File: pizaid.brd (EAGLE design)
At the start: 55.2 x 49.5 mm, 37 parts, among them X1 S4B-ZR

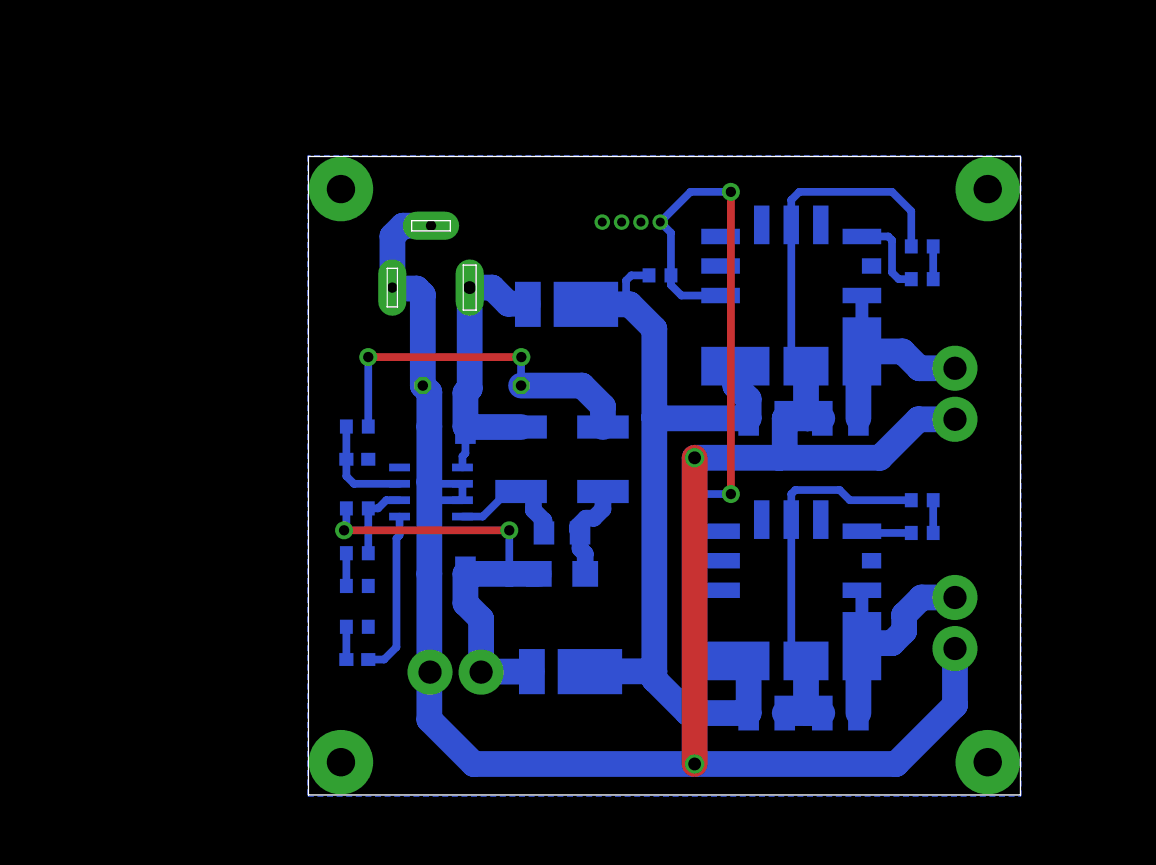
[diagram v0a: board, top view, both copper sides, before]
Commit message: supported Raspberry Pi model B+
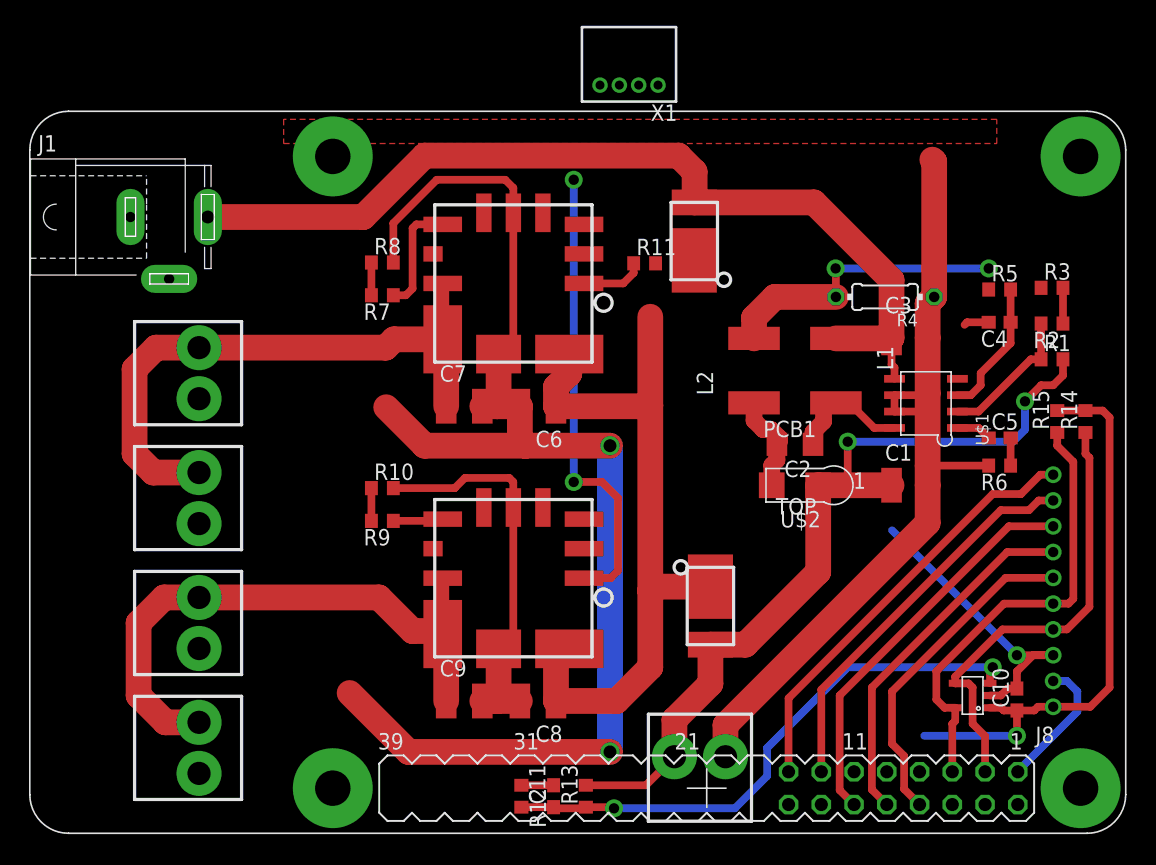
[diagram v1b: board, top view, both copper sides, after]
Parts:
- removed U$11, U$12, U$13, U$3: M2, pizaid:M2
- added C10, C11: (no value), rcl:C0603
- added PCB1: RASPBERRY_PI_B+, pizaid:RASPBERRY_PI_B+
- added R12, R13, R14, R15: (no value), rcl:R0603
- added S1: 10B-PH, con-jst:S10B-PH
- added U$14, U$15: B2P-VH, pizaid:B2P-VH
- added U$16: MCP3021, pizaid:SOT-23
- moved U$9 59.4 mm to (16.6, 10.0), flipped to the top
- moved U$8 59.2 mm to (16.6, 29.4), flipped to the top
- moved R3 58.6 mm to (82.7, 45.7), flipped to the top
- moved R2 56.8 mm to (82.7, 42.9), flipped to the top
- moved R1 55.1 mm to (82.7, 40.1), flipped to the top
- moved C5 52.7 mm to (78.7, 34.0), flipped to the top
- moved R6 51.4 mm to (78.7, 31.9), flipped to the top
- moved C4 50.9 mm to (78.7, 43.0), flipped to the top
- moved R5 50.9 mm to (78.7, 45.5), flipped to the top
- moved R7 41.9 mm to (30.8, 45.1), flipped to the top
- moved R8 41.9 mm to (30.8, 47.6), flipped to the top
- moved R10 41.9 mm to (30.8, 30.1), flipped to the top
- moved R9 41.9 mm to (30.8, 27.6), flipped to the top
- moved U$1 39.0 mm to (72.9, 36.7), flipped to the top
- moved C1 36.5 mm to (71.7, 30.4), flipped to the top
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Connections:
- new net 3V3@1: PCB1.1, S1.P$2
- new net 5V0@2: C10.1, C9.1, PCB1.2, PCB1.4, R14.2, R15.2, S1.P$1, U$14.P$1, U$16.P$1, U$7.P$4, U$7.P$5, U$9.P$1
- new net GND@1: PCB1.9
- new net GND@4: PCB1.14, PCB1.6
- new net JNET: C7.1, U$15.P$1, U$6.P$4, U$6.P$5, U$8.P$1
- new net N$13: PCB1.8, S1.P$6
- new net N$16: PCB1.5, R15.1, S1.P$5, U$16.P$5
- new net N$20: PCB1.3, R14.1, S1.P$4, U$16.P$4
- new net N$21: PCB1.10, S1.P$7
- new net N$22: PCB1.12, S1.P$8
- new net N$23: PCB1.13, S1.P$9
- net GND: now also C10.2, C11.2, PCB1.PE_BL, PCB1.PE_BR, PCB1.PE_TL, PCB1.PE_TR, R12.1, S1.P$3, U$14.P$2, U$15.P$2, U$16.P$2; no longer U$11.P$1, U$12.P$1, U$13.P$1, U$3.P$1
- net N$19: now also C11.1, R12.2, R13.1, U$16.P$3; no longer C7.1, U$6.P$4, U$6.P$5, U$8.P$1
- net N$3: now also R13.2
- net N$9: now also PCB1.15, S1.P$10; no longer C9.1, U$7.P$4, U$7.P$5, U$9.P$1
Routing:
- net 5V0@2: track 0.00 -> 90.9 mm, vias 0 -> 1
- net VCC: track 23.6 -> 72.5 mm
- net JNET: track 0.00 -> 46.7 mm
- net N$16: track 0.00 -> 35.3 mm
- net N$20: track 0.00 -> 35.2 mm
- net N$22: track 0.00 -> 30.9 mm
- net N$23: track 0.00 -> 30.4 mm
- net N$3: track 35.7 -> 65.5 mm
- net N$21: track 0.00 -> 28.0 mm
- net N$19: track 17.4 -> 44.1 mm, vias 0 -> 2
- net N$13: track 0.00 -> 25.8 mm
- net GND: track 207.2 -> 221.7 mm, vias 2 -> 3
- net N$9: track 19.2 -> 33.4 mm
- net N$12: track 51.8 -> 40.8 mm
- net 3V3@1: track 0.00 -> 10.4 mm
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- added copper zone on layer 1, net GND
- removed copper zone on layer 16, net GND
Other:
- board size 55.2 x 49.5 mm -> 6.9 x 6.9 mm

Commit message: added gerber and con-jst.lbr
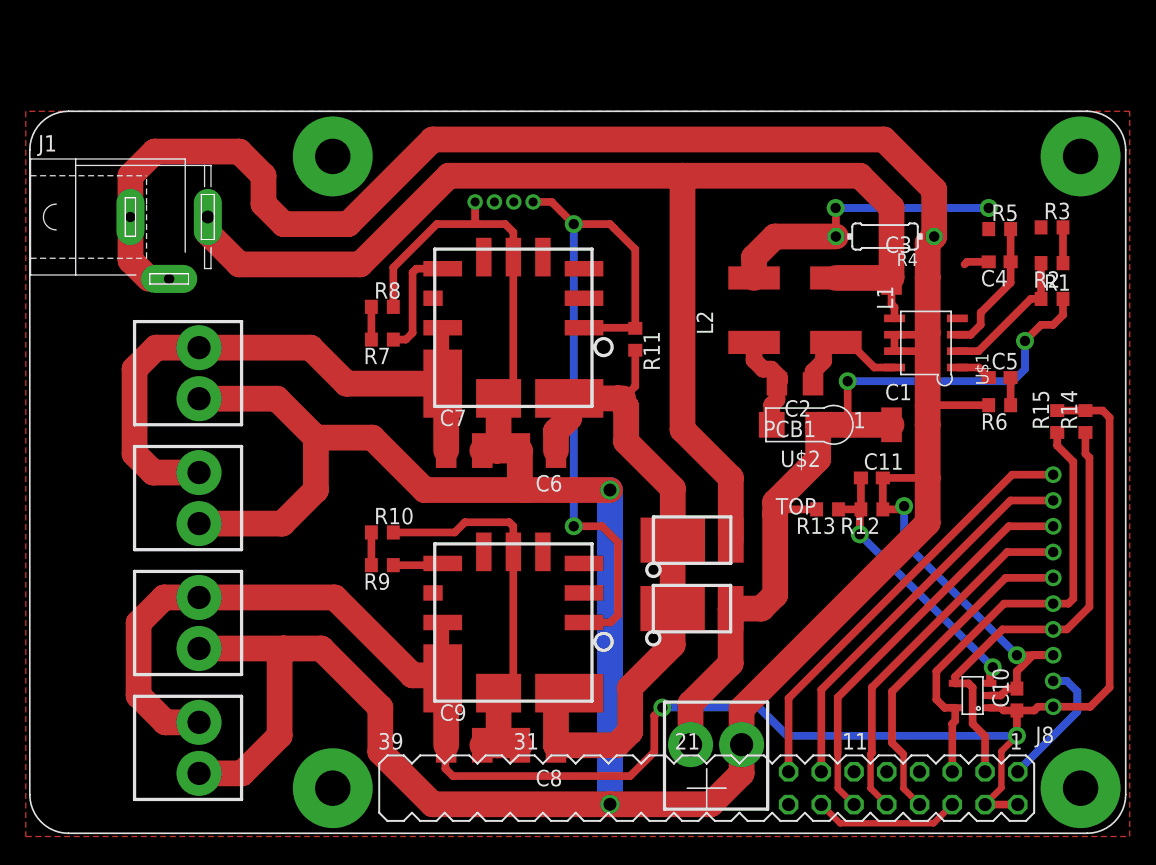
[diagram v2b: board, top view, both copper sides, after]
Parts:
- moved R12 35.1 mm to (68.8, 28.5), turned to 180 degrees
- moved C11 34.9 mm to (68.8, 30.9), turned to 0 degrees
- moved R13 29.1 mm to (65.3, 28.5), turned to 180 degrees
- moved U$5 23.2 mm to (54.8, 26.1), turned to 180 degrees
- moved X1 13.3 mm to (40.2, 52.3), flipped to the bottom
- moved R11 5.94 mm to (50.4, 41.7), turned to 270 degrees
- moved C2 4.69 mm to (62.8, 38.2)
- moved C3 4.69 mm to (71.7, 46.5)
- moved C4 4.69 mm to (78.7, 47.7)
- moved C5 4.69 mm to (78.7, 38.7)
- moved L1 4.69 mm to (66.0, 43.9)
- moved L2 4.69 mm to (59.6, 43.9)
- moved R1 4.69 mm to (82.7, 44.8)
- moved R2 4.69 mm to (82.7, 47.6)
- moved R3 4.69 mm to (82.7, 50.4)
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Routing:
- net GND: track 221.7 -> 385.4 mm, vias 3 -> 4
- net 5V0@2: track 90.9 -> 145.3 mm, vias 1 -> 2
- net VCC: track 72.5 -> 102.0 mm
- net N$19: track 44.1 -> 22.1 mm
- net N$12: track 40.8 -> 55.5 mm
- net GND@4: track 0.00 -> 11.4 mm
- net N$8: track 56.7 -> 52.4 mm
- net N$3: track 65.5 -> 64.1 mm
- net JNET: track 46.7 -> 47.6 mm

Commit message: added part info
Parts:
- C1: value (none) -> 22u
- C10, C11, C5: value (none) -> 0.1u
- C2: value (none) -> 2.2u
- C4: value (none) -> 0.22u
- C6, C8: value (none) -> 22u25V
- C7, C9: value (none) -> 22u16V
- L1, L2: value (none) -> 33u
- R1: value (none) -> 100k
- R10, R8: value (none) -> 330
- R12, R13, R2: value (none) -> 10k
- R14, R15, R3: value (none) -> 2.2k
- R4: value (none) -> 0.2
- R5: value (none) -> 24
- R6, R7, R9: value (none) -> 1k
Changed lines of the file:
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@@
 <elements>
 <element name="U$1" library="pizaid" package="SOP8" value="LT1512CS8" x="72.945" y="41.4075" rot="R90"/>
-<element name="R1" library="rcl" package="R0603" value="" x="82.7225" y="44.825"/>
-<element name="R2" library="rcl" package="R0603" value="" x="82.7225" y="47.5975" rot="R180"/>
-<element name="R3" library="rcl" package="R0603" value="" x="82.7225" y="50.37"/>
-<element name="R4" library="rcl" package="0204/7" value="" x="69.77" y="49.6625" rot="R180"/>
-<element name="R5" library="rcl" package="R0603" value="" x="78.66" y="50.2375"/>
-<element name="R6" library="rcl" package="R0603" value="" x="78.66" y="36.58" rot="R180"/>
-<element name="C1" library="rcl" package="C3225" value="" x="71.675" y="35.0575"/>
-<element name="C2" library="rcl" package="C3216" value="" x="62.785" y="38.2325" rot="R180"/>
+<element name="R1" library="rcl" package="R0603" value="100k" x="82.7225" y="44.825"/>
+<element name="R2" library="rcl" package="R0603" value="10k" x="82.7225" y="47.5975" rot="R180"/>
+<element name="R3" library="rcl" package="R0603" value="2.2k" x="82.7225" y="50.37"/>
+<element name="R4" library="rcl" package="0204/7" value="0.2" x="69.77" y="49.6625" rot="R180"/>
+<element name="R5" library="rcl" package="R0603" value="24" x="78.66" y="50.2375"/>
+<element name="R6" library="rcl" package="R0603" value="1k" x="78.66" y="36.58" rot="R180"/>
+<element name="C1" library="rcl" package="C3225" value="22u" x="71.675" y="35.0575"/>
+<element name="C2" library="rcl" package="C3216" value="2.2u" x="62.785" y="38.2325" rot="R180"/>
 <element name="C3" library="rcl" package="C3225" value="22u" x="71.675" y="46.4875"/>
-<element name="C4" library="rcl" package="C0603" value="" x="78.66" y="47.6975" rot="R180"/>
-<element name="C5" library="rcl" package="C0603" value="" x="78.66" y="38.7275"/>
-<element name="L1" library="rcl" package="L5650M" value="" x="65.96" y="43.9475" rot="R270"/>
-<element name="L2" library="rcl" package="L5650M" value="" x="59.61" y="43.9475" rot="R90"/>
+<element name="C4" library="rcl" package="C0603" value="0.22u" x="78.66" y="47.6975" rot="R180"/>
+<element name="C5" library="rcl" package="C0603" value="0.1u" x="78.66" y="38.7275"/>
+<element name="L1" library="rcl" package="L5650M" value="33u" x="65.96" y="43.9475" rot="R270"/>
+<element name="L2" library="rcl" package="L5650M" value="33u" x="59.61" y="43.9475" rot="R90"/>
 <element name="U$2" library="pizaid" package="SOD-123FL" value="SS2040FL" x="62.785" y="35.0575" rot="R180"/>
 <element name="J1" library="pizaid" package="SPC4077" value="" x="14.2425" y="51.175">
@@
 <element name="U$6" library="pizaid" package="OKL-T/6" value="OKL-T/6" x="40.9425" y="42.585" rot="R180"/>
 <element name="U$7" library="pizaid" package="OKL-T/6" value="OKL-T/6" x="40.9425" y="19.725" rot="R180"/>
-<element name="C6" library="rcl" package="C3225" value="" x="42.8475" y="33.06" rot="R180"/>
-<element name="C7" library="rcl" package="C3225" value="" x="37.1325" y="33.06"/>
-<element name="C8" library="rcl" package="C3225" value="" x="42.8475" y="10.2" rot="R180"/>
-<element name="C9" library="rcl" package="C3225" value="" x="37.1325" y="10.2"/>
-<element name="R7" library="rcl" package="R0603" value="" x="30.7825" y="41.6675" rot="R180"/>
-<element name="R8" library="rcl" package="R0603" value="" x="30.7825" y="44.2075"/>
-<element name="R9" library="rcl" package="R0603" value="" x="30.7825" y="24.17" rot="R180"/>
-<element name="R10" library="rcl" package="R0603" value="" x="30.7825" y="26.71"/>
+<element name="C6" library="rcl" package="C3225" value="22u25V" x="42.8475" y="33.06" rot="R180"/>
+<element name="C7" library="rcl" package="C3225" value="22u16V" x="37.1325" y="33.06"/>
+<element name="C8" library="rcl" package="C3225" value="22u25V" x="42.8475" y="10.2" rot="R180"/>
+<element name="C9" library="rcl" package="C3225" value="22u16V" x="37.1325" y="10.2"/>
+<element name="R7" library="rcl" package="R0603" value="1k" x="30.7825" y="41.6675" rot="R180"/>
+<element name="R8" library="rcl" package="R0603" value="330" x="30.7825" y="44.2075"/>
+<element name="R9" library="rcl" package="R0603" value="1k" x="30.7825" y="24.17" rot="R180"/>
+<element name="R10" library="rcl" package="R0603" value="330" x="30.7825" y="26.71"/>
 <element name="X1" library="con-jst" package="S4B-ZR" value="S4B-ZR" x="40.225" y="52.3425" rot="MR180">
 <attribute name="OC_NEWARK" value="38K8076" x="40.225" y="52.3425" size="1.778" layer="28" rot="MR180" display="off"/>
@@
 <element name="U$15" library="pizaid" package="B2P-VH" value="B2P-VH" x="16.5625" y="39.0625" rot="R270"/>
 <element name="U$16" library="pizaid" package="SOT-23" value="MCP3021" x="76.5625" y="14.0625" rot="R90"/>
-<element name="C10" library="rcl" package="C0603" value="" x="80" y="13.75" rot="R90"/>
-<element name="C11" library="rcl" package="C0603" value="" x="68.75" y="30.9375"/>
-<element name="R12" library="rcl" package="R0603" value="" x="68.75" y="28.5" rot="R180"/>
-<element name="R13" library="rcl" package="R0603" value="" x="65.3125" y="28.5" rot="R180"/>
-<element name="R14" library="rcl" package="R0603" value="" x="85.3125" y="35.3125" rot="R90"/>
-<element name="R15" library="rcl" package="R0603" value="" x="83.125" y="35.3125" rot="R90"/>
+<element name="C10" library="rcl" package="C0603" value="0.1u" x="80" y="13.75" rot="R90"/>
+<element name="C11" library="rcl" package="C0603" value="0.1u" x="68.75" y="30.9375"/>
+<element name="R12" library="rcl" package="R0603" value="10k" x="68.75" y="28.5" rot="R180"/>
+<element name="R13" library="rcl" package="R0603" value="10k" x="65.3125" y="28.5" rot="R180"/>
+<element name="R14" library="rcl" package="R0603" value="2.2k" x="85.3125" y="35.3125" rot="R90"/>
+<element name="R15" library="rcl" package="R0603" value="2.2k" x="83.125" y="35.3125" rot="R90"/>
 <element name="PCB1" library="pizaid" package="RASPBERRY_PI_B+" value="RASPBERRY_PI_B+" x="88.4375" y="59.375" rot="R180"/>
 </elements>

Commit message: changed dcjack
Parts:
- removed J1: (no value), pizaid:SPC4077
- added X2: DCJACK-R, kamiki-dcjack:2DC-0005D100-R
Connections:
- net GND: now also X2.2, X2.3; no longer J1.1, J1.2
- net VCC: now also X2.1; no longer J1.3
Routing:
- net VCC: track 102.0 -> 101.5 mm
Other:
- board outline removed
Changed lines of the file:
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@@
 <element name="L2" library="rcl" package="L5650M" value="33u" x="59.61" y="43.9475" rot="R90"/>
 <element name="U$2" library="pizaid" package="SOD-123FL" value="SS2040FL" x="62.785" y="35.0575" rot="R180"/>
-<element name="J1" library="pizaid" package="SPC4077" value="" x="14.2425" y="51.175">
-<attribute name="OC_NEWARK" value="unknown" x="14.2425" y="51.175" size="1.778" layer="27" display="off"/>
-<attribute name="MPN" value="" x="14.2425" y="51.175" size="1.778" layer="27" display="off"/>
-<attribute name="MF" value="" x="14.2425" y="51.175" size="1.778" layer="27" display="off"/>
-<attribute name="OC_FARNELL" value="unknown" x="14.2425" y="51.175" size="1.778" layer="27" display="off"/>
-</element>
 <element name="U$4" library="pizaid" package="POWERDI5" value="SBR15U50" x="54.795" y="20.8025" rot="R180"/>
 <element name="U$5" library="pizaid" package="POWERDI5" value="SBR15U50" x="54.8075" y="26.1125" rot="R180"/>
@@
 <element name="R15" library="rcl" package="R0603" value="2.2k" x="83.125" y="35.3125" rot="R90"/>
 <element name="PCB1" library="pizaid" package="RASPBERRY_PI_B+" value="RASPBERRY_PI_B+" x="88.4375" y="59.375" rot="R180"/>
+<element name="X2" library="kamiki-dcjack" package="2DC-0005D100-R" value="DCJACK-R" x="13.4375" y="51.5625"/>
 </elements>
 <signals>
@@
 <contactref element="C1" pad="2"/>
 <contactref element="R3" pad="1"/>
-<contactref element="J1" pad="2"/>
-<contactref element="J1" pad="1"/>
 <contactref element="U$6" pad="P$3"/>
 <contactref element="U$7" pad="P$3"/>
@@
 <wire x1="25.625" y1="34.0625" x2="22.605" y2="37.0825" width="2" layer="1"/>
 <wire x1="16.5625" y1="37.0825" x2="22.605" y2="37.0825" width="2" layer="1"/>
-<wire x1="11.2425" y1="51.175" x2="11.2425" y2="54.3675" width="2" layer="1"/>
 <wire x1="11.2425" y1="54.3675" x2="13.125" y2="56.25" width="2" layer="1"/>
 <wire x1="13.125" y1="56.25" x2="19.6875" y2="56.25" width="2" layer="1"/>
@@
 <wire x1="69.6875" y1="57.1875" x2="73.58" y2="53.295" width="2" layer="1"/>
 <wire x1="73.58" y1="49.6625" x2="73.58" y2="53.295" width="2" layer="1"/>
-<wire x1="12.6875" y1="46.375" x2="11.25" y2="47.8125" width="2" layer="1"/>
-<wire x1="11.25" y1="47.8125" x2="11.25" y2="51.1825" width="2" layer="1"/>
-<wire x1="11.25" y1="51.5625" x2="11.25" y2="51.1825" width="2" layer="1"/>
-<wire x1="11.25" y1="51.1825" x2="11.2425" y2="51.175" width="2" layer="1"/>
 <wire x1="25.625" y1="34.0625" x2="30" y2="34.0625" width="2" layer="1"/>
 <wire x1="48.4375" y1="5.625" x2="56.25" y2="5.625" width="2" layer="1"/>
@@
 <wire x1="37.975" y1="52.3425" x2="37.975" y2="50.775" width="0.6" layer="1"/>
 <wire x1="37.975" y1="50.775" x2="38.125" y2="50.625" width="0.6" layer="1"/>
+<contactref element="X2" pad="2"/>
+<contactref element="X2" pad="3"/>
+<wire x1="11.1875" y1="51.5625" x2="11.2425" y2="51.6175" width="2" layer="1"/>
+<wire x1="11.2425" y1="51.6175" x2="11.2425" y2="54.3675" width="2" layer="1"/>
+<wire x1="11.1875" y1="51.5625" x2="11.1875" y2="49.7625" width="2" layer="1"/>
+<wire x1="11.1875" y1="49.7625" x2="14.1875" y2="46.7625" width="2" layer="1"/>
 <wire x1="41.875" y1="30" x2="40.625" y2="27.5" width="0" layer="19" extent="1-1"/>
 </signal>
@@
 <contactref element="L1" pad="1"/>
 <contactref element="U$1" pad="5"/>
-<contactref element="J1" pad="3"/>
 <contactref element="U$5" pad="P$2"/>
 <wire x1="65.96" y1="46.4475" x2="70.235" y2="46.4475" width="2" layer="1"/>
@@
 <wire x1="54.0625" y1="54.375" x2="35.9375" y2="54.375" width="2" layer="1"/>
 <wire x1="35.9375" y1="54.375" x2="29.0625" y2="47.5" width="2" layer="1"/>
-<wire x1="29.0625" y1="47.5" x2="19.6875" y2="47.5" width="2" layer="1"/>
-<wire x1="19.6875" y1="47.5" x2="17.2425" y2="49.945" width="2" layer="1"/>
-<wire x1="17.2425" y1="51.175" x2="17.2425" y2="49.945" width="2" layer="1"/>
+<contactref element="X2" pad="1"/>
+<wire x1="17.1875" y1="51.5625" x2="21.25" y2="47.5" width="2" layer="1"/>
+<wire x1="21.25" y1="47.5" x2="29.0625" y2="47.5" width="2" layer="1"/>
 </signal>
 <signal name="N$2">
